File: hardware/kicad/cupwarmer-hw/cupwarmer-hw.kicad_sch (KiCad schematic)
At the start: 0 parts

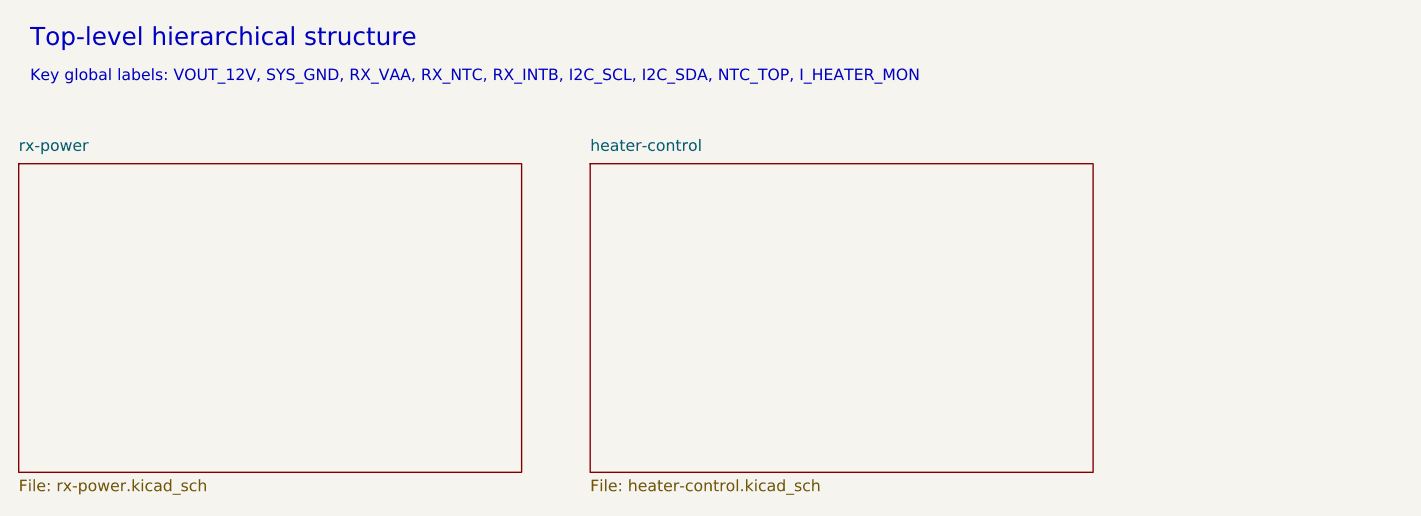
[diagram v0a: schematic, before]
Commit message: Add heater harness NTC routing
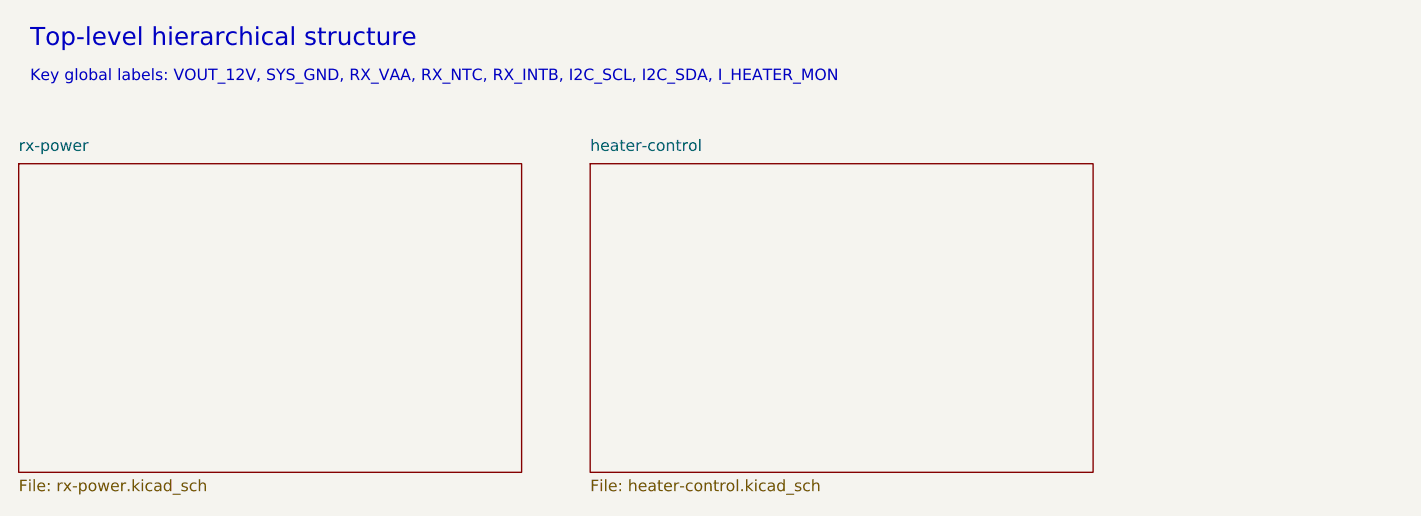
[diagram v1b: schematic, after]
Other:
- note added: "Key global labels: VOUT_12V, SYS_GND, RX_VAA, RX_NTC, RX_INTB, I2C_SCL, I2C_SDA, I_HEATER_MON"
- note removed: "Key global labels: VOUT_12V, SYS_GND, RX_VAA, RX_NTC, RX_INTB, I2C_SCL, I2C_SDA, NTC_TOP, I_HEATER_MON"
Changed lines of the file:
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@@
 		)
 	)
-	(text "Key global labels: VOUT_12V, SYS_GND, RX_VAA, RX_NTC, RX_INTB, I2C_SCL, I2C_SDA, NTC_TOP, I_HEATER_MON"
+	(text "Key global labels: VOUT_12V, SYS_GND, RX_VAA, RX_NTC, RX_INTB, I2C_SCL, I2C_SDA, I_HEATER_MON"
 		(exclude_from_sim no)
 		(at 39.37 35.56 0)

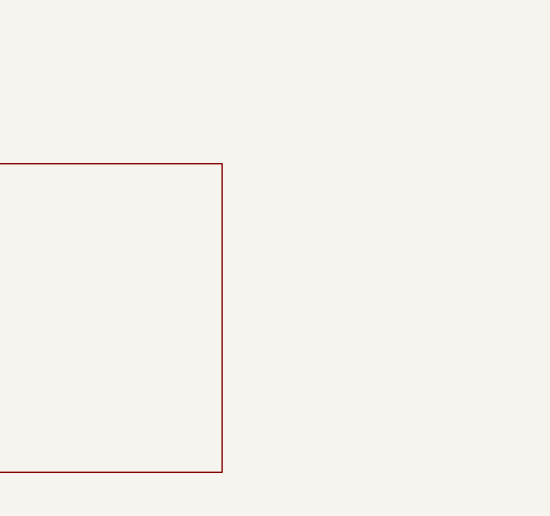
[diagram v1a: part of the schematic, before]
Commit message: Add schematic mounting holes for board parity
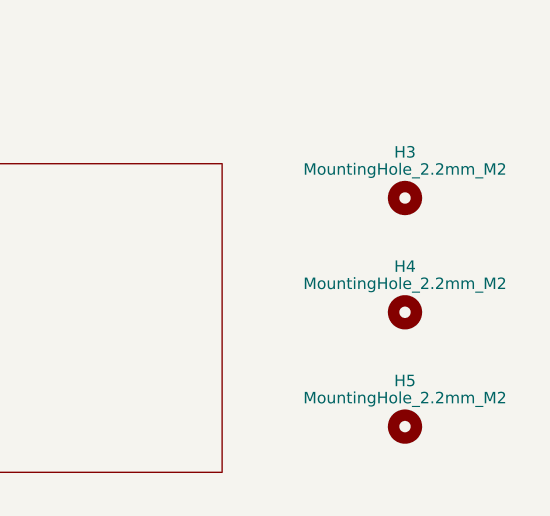
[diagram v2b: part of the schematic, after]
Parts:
- added H3, H4, H5: MountingHole_2.2mm_M2, MountingHole:MountingHole_2.2mm_M2, symbol Mechanical:MountingHole
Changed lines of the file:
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@@
+		)
+	)
+	(symbol
+		(lib_id "Mechanical:MountingHole")
+		(at 177.8 60.96 0)
+		(unit 1)
+		(body_style 1)
+		(exclude_from_sim no)
+		(in_bom no)
+		(on_board yes)
+		(in_pos_files no)
+		(dnp no)
+		(property "Reference" "H4"
+			(at 177.8 55.88 0)
+			(show_name no)
+			(do_not_autoplace no)
+			(effects
+				(font
+					(size 1.27 1.27)
+				)
+			)
+		)
+		(property "Value" "MountingHole_2.2mm_M2"
+			(at 177.8 57.785 0)
+			(show_name no)
+			(do_not_autoplace no)
+			(effects
+				(font
+					(size 1.27 1.27)
+				)
+			)
+		)
+		(property "Footprint" "MountingHole:MountingHole_2.2mm_M2"
+			(at 177.8 60.96 0)
+			(hide yes)
+			(show_name no)
+			(do_not_autoplace no)
+			(effects
+				(font
+					(size 1.27 1.27)
+				)
+			)
+		)
+		(property "Datasheet" ""
+			(at 177.8 60.96 0)
+			(hide yes)
+			(show_name no)
+			(do_not_autoplace no)
+			(effects
+				(font
+					(size 1.27 1.27)
+				)
+			)
+		)
+		(property "Description" "PCB-only NPTH mounting hole"
+			(at 177.8 60.96 0)
+			(hide yes)
+			(show_name no)
+			(do_not_autoplace no)
+			(effects
+				(font
+					(size 1.27 1.27)
+				)
+			)
+		)
+		(instances
+			(project "cupwarmer-hw"
+				(path "/f3c63676-f392-4700-9f58-a6787e1eb284"
+					(reference "H4")
+					(unit 1)
+				)
+			)
+		)
+	)
+	(symbol
+		(lib_id "Mechanical:MountingHole")
+		(at 177.8 73.66 0)
+		(unit 1)
+		(body_style 1)
+		(exclude_from_sim no)
+		(in_bom no)
+		(on_board yes)
+		(in_pos_files no)
+		(dnp no)
+		(property "Reference" "H5"
+			(at 177.8 68.58 0)
+			(show_name no)
+			(do_not_autoplace no)
+			(effects
+				(font
+					(size 1.27 1.27)
+				)
+			)
+		)
+		(property "Value" "MountingHole_2.2mm_M2"
+			(at 177.8 70.485 0)
+			(show_name no)
+			(do_not_autoplace no)
+			(effects
+				(font
+					(size 1.27 1.27)
+				)
+			)
+		)
+		(property "Footprint" "MountingHole:MountingHole_2.2mm_M2"
+			(at 177.8 73.66 0)
+			(hide yes)
+			(show_name no)
+			(do_not_autoplace no)
+			(effects
+				(font
+					(size 1.27 1.27)
+				)
+			)
+		)
+		(property "Datasheet" ""
+			(at 177.8 73.66 0)
+			(hide yes)
+			(show_name no)
+			(do_not_autoplace no)
+			(effects
+				(font
+					(size 1.27 1.27)
+				)
+			)
+		)
+		(property "Description" "PCB-only NPTH mounting hole"
+			(at 177.8 73.66 0)
+			(hide yes)
+			(show_name no)
+			(do_not_autoplace no)
+			(effects
+				(font
+					(size 1.27 1.27)
+				)
+			)
+		)
+		(instances
+			(project "cupwarmer-hw"
+				(path "/f3c63676-f392-4700-9f58-a6787e1eb284"
+					(reference "H5")
+					(unit 1)
+				)
+			)
+		)
+	)
+	(symbol
+		(lib_id "Mechanical:MountingHole")
+		(at 177.8 48.26 0)
+		(unit 1)
+		(body_style 1)
+		(exclude_from_sim no)
+		(in_bom no)
+		(on_board yes)
+		(in_pos_files no)
+		(dnp no)
+		(property "Reference" "H3"
+			(at 177.8 43.18 0)
+			(show_name no)
+			(do_not_autoplace no)
+			(effects
+				(font
+					(size 1.27 1.27)
+				)
+			)
+		)
+		(property "Value" "MountingHole_2.2mm_M2"
+			(at 177.8 45.085 0)
+			(show_name no)
+			(do_not_autoplace no)
+			(effects
+				(font
+					(size 1.27 1.27)
+				)
+			)
+		)
+		(property "Footprint" "MountingHole:MountingHole_2.2mm_M2"
+			(at 177.8 48.26 0)
+			(hide yes)
+			(show_name no)
+			(do_not_autoplace no)
+			(effects
+				(font
+					(size 1.27 1.27)
+				)
+			)
+		)
+		(property "Datasheet" ""
+			(at 177.8 48.26 0)
+			(hide yes)
+			(show_name no)
+			(do_not_autoplace no)
+			(effects
+				(font
+					(size 1.27 1.27)
+				)
+			)
+		)
+		(property "Description" "PCB-only NPTH mounting hole"
+			(at 177.8 48.26 0)
+			(hide yes)
+			(show_name no)
+			(do_not_autoplace no)
+			(effects
+				(font
+					(size 1.27 1.27)
+				)
+			)
+		)
+		(instances
+			(project "cupwarmer-hw"
+				(path "/f3c63676-f392-4700-9f58-a6787e1eb284"
+					(reference "H3")
+					(unit 1)
+				)
+			)
 		)
 	)
